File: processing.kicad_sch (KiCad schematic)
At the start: 58 parts, among them IC4 MT29F2G01ABAGDWB-IT_G_TR, IC5 MT29F2G01ABAGDWB-IT_G_TR, IC6 XMC7200D-E272K8384AA, IC7 DS90LV011AHMF_NOPB, Q1 ZXT849K, Y1 DSC1101DM2-012.0000, Y2 DSC1101DM2-125.0000T

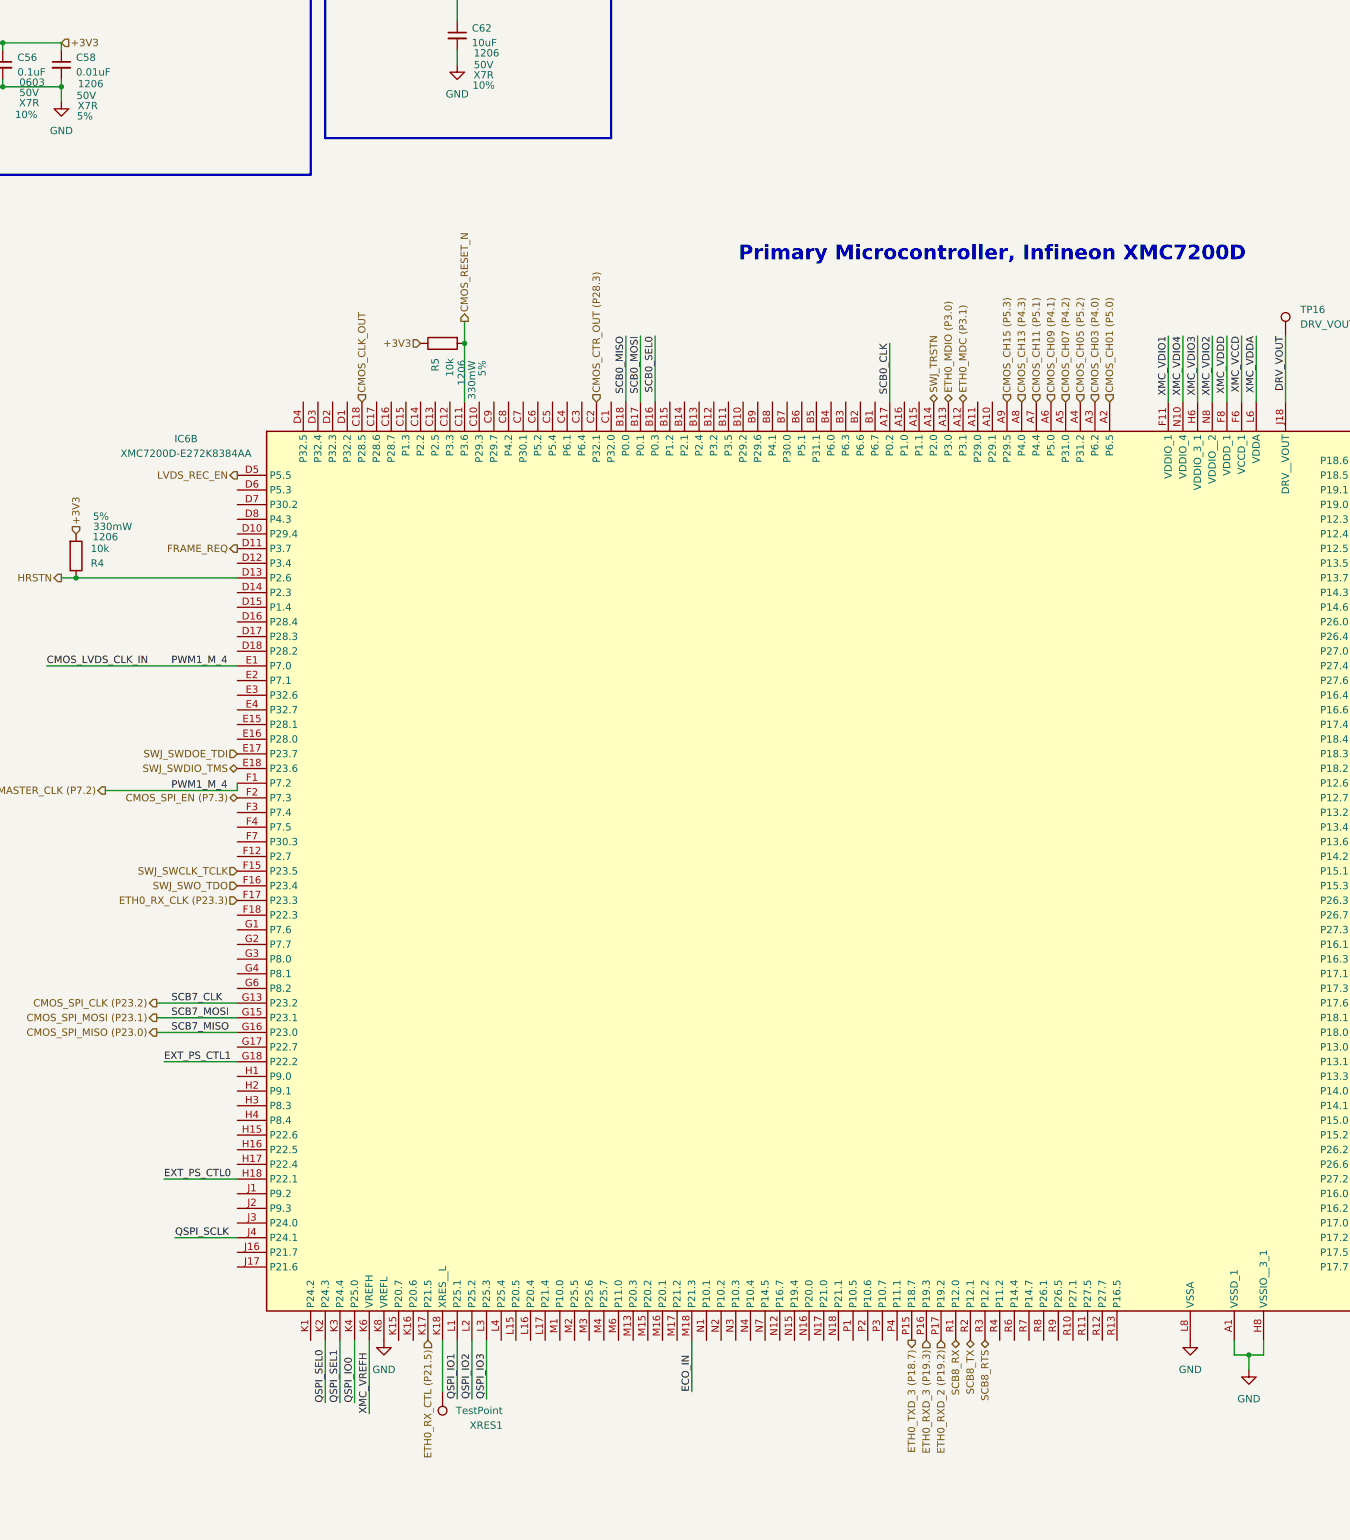
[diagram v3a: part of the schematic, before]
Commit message: Ready to order
Still unsure about 100uF cap
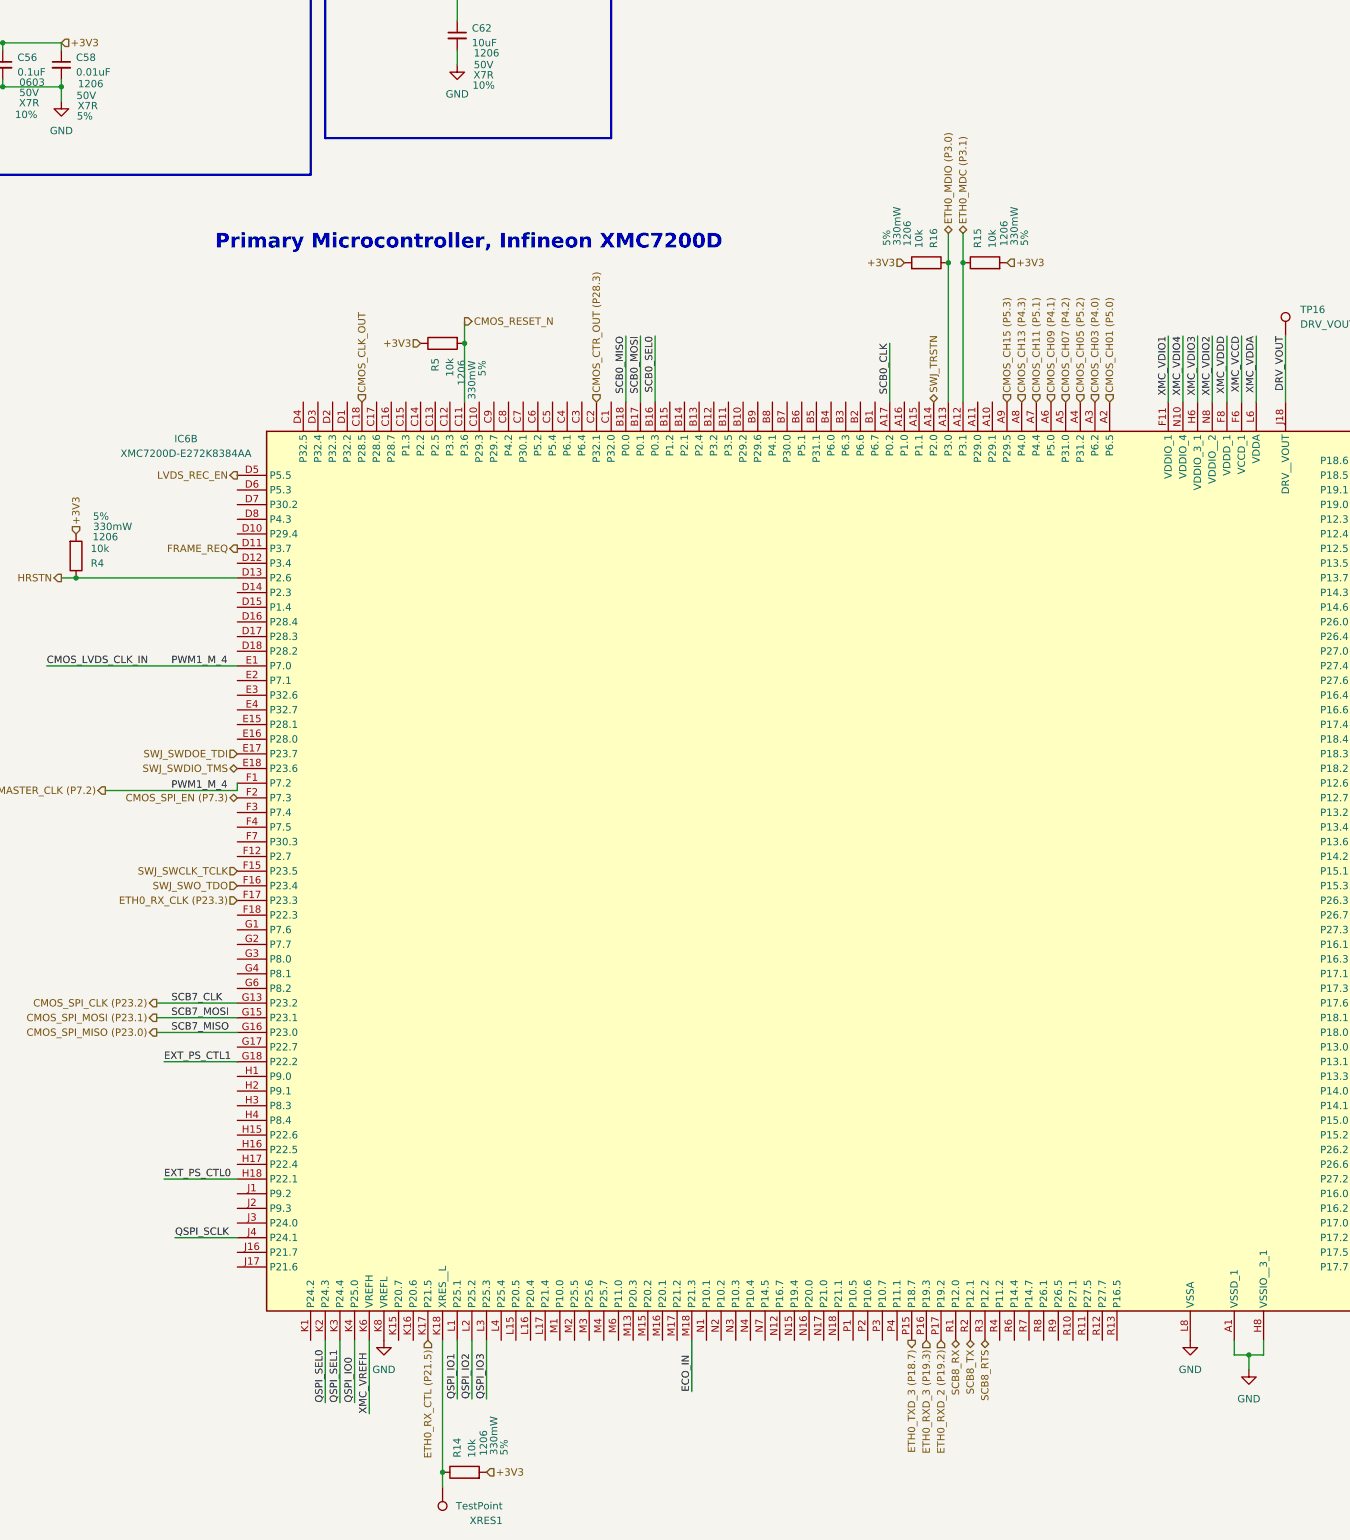
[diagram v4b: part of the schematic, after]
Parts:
- added R14, R15, R16: 10k, Resistor_SMD:R_1206_3216Metric, symbol Device:R
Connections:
- net +3V3: now also R14.2, R15.2, R16.2
- net ETH0_MDC (P3.1): now also R15.1
- net ETH0_MDIO (P3.0): now also R16.1
- net at IC6.K18 (XRES__L), XRES1.1: now also R14.1
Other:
- moved on the sheet: XRES1

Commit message: Labeled test pads; marked tantalums with lines for cathode; found suitable tantalum for 100 uF
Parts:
- DRV_VOUT1: renamed from TP16; value DRV_VOUT -> DRV_VOUT1
- renumbered TP15 to QSPI_IO0, TP11 to QSPI_IO1, TP12 to QSPI_IO2, TP13 to QSPI_IO3, TP14 to QSPI_SCLK1, TP10 to QSPI_SEL0, TP17 to QSPI_SEL1
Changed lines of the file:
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@@
 		(on_board yes)
 		(dnp no)
-		(fields_autoplaced yes)
-		(property "Reference" "TP15"
+		(property "Reference" "QSPI_IO0"
 			(at 93.98 113.0299 90)
 			(effects
@@
 			(project "S25-26"
 				(path "/6f4563ef-8a79-4567-b913-33c6dfb42b56/e295881b-793d-44b2-856b-25e9d19ba3af"
-					(reference "TP15")
+					(reference "QSPI_IO0")
 					(unit 1)
 				)
@@
 		(on_board yes)
 		(dnp no)
-		(fields_autoplaced yes)
-		(property "Reference" "TP13"
+		(property "Reference" "QSPI_IO3"
 			(at 93.98 105.4099 90)
 			(effects
@@
 			(project "S25-26"
 				(path "/6f4563ef-8a79-4567-b913-33c6dfb42b56/e295881b-793d-44b2-856b-25e9d19ba3af"
-					(reference "TP13")
+					(reference "QSPI_IO3")
 					(unit 1)
 				)
@@
 		(on_board yes)
 		(dnp no)
-		(fields_autoplaced yes)
-		(property "Reference" "TP17"
+		(property "Reference" "QSPI_SEL1"
 			(at 17.78 124.9679 0)
 			(effects
@@
 			(project "S25-26"
 				(path "/6f4563ef-8a79-4567-b913-33c6dfb42b56/e295881b-793d-44b2-856b-25e9d19ba3af"
-					(reference "TP17")
+					(reference "QSPI_SEL1")
 					(unit 1)
 				)
@@
 		(on_board yes)
 		(dnp no)
-		(fields_autoplaced yes)
-		(property "Reference" "TP10"
+		(property "Reference" "QSPI_SEL0"
 			(at 17.78 95.7579 0)
 			(effects
@@
 			(project "S25-26"
 				(path "/6f4563ef-8a79-4567-b913-33c6dfb42b56/e295881b-793d-44b2-856b-25e9d19ba3af"
-					(reference "TP10")
+					(reference "QSPI_SEL0")
 					(unit 1)
 				)
@@
 		(on_board yes)
 		(dnp no)
-		(fields_autoplaced yes)
-		(property "Reference" "TP12"
+		(property "Reference" "QSPI_IO2"
 			(at 22.86 121.9199 90)
 			(effects
@@
 			(project "S25-26"
 				(path "/6f4563ef-8a79-4567-b913-33c6dfb42b56/e295881b-793d-44b2-856b-25e9d19ba3af"
-					(reference "TP12")
+					(reference "QSPI_IO2")
 					(unit 1)
 				)
@@
 		(on_board yes)
 		(dnp no)
-		(fields_autoplaced yes)
-		(property "Reference" "TP14"
+		(property "Reference" "QSPI_SCLK1"
 			(at 93.98 109.2199 90)
 			(effects
@@
 			(project "S25-26"
 				(path "/6f4563ef-8a79-4567-b913-33c6dfb42b56/e295881b-793d-44b2-856b-25e9d19ba3af"
-					(reference "TP14")
+					(reference "QSPI_SCLK1")
 					(unit 1)
 				)
@@
 		(on_board yes)
 		(dnp no)
-		(fields_autoplaced yes)
-		(property "Reference" "TP11"
+		(property "Reference" "QSPI_IO1"
 			(at 17.78 117.6019 0)
 			(effects
@@
 			(project "S25-26"
 				(path "/6f4563ef-8a79-4567-b913-33c6dfb42b56/e295881b-793d-44b2-856b-25e9d19ba3af"
-					(reference "TP11")
+					(reference "QSPI_IO1")
 					(unit 1)
 				)
@@
 		(on_board yes)
 		(dnp no)
-		(fields_autoplaced yes)
-		(property "Reference" "TP16"
+		(property "Reference" "DRV_VOUT1"
 			(at 375.92 107.1879 0)
 			(effects
@@
 			)
 		)
-		(property "Value" "DRV_VOUT"
+		(property "Value" "DRV_VOUT1"
 			(at 375.92 109.7279 0)
 			(effects
@@
 			(project "S25-26"
 				(path "/6f4563ef-8a79-4567-b913-33c6dfb42b56/e295881b-793d-44b2-856b-25e9d19ba3af"
-					(reference "TP16")
+					(reference "DRV_VOUT1")
 					(unit 1)
 				)

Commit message: Beginning of V3
Long way to go
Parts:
- Q1: footprint Package_TO_SOT_SMD:TO-252-3_TabPin4 -> CustomFootprintLibrary:TO-252-3_TabPin4
- R6: footprint Resistor_SMD:R_0805_2012Metric -> Resistor_SMD:R_1206_3216Metric
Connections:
- net XRES: now reaches IC6.K18 (XRES__L), R14.1, XRES1.1
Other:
- moved on the sheet: XRES1
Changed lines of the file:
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@@
 		)
 	)
+	(hierarchical_label "XRES"
+		(shape input)
+		(at 227.33 311.15 270)
+		(effects
+			(font
+				(size 1.27 1.27)
+			)
+			(justify right)
+		)
+	)
 	(hierarchical_label "+3V3"
 		(shape input)
@@
 			)
 		)
-		(property "Footprint" "Resistor_SMD:R_0805_2012Metric"
+		(property "Footprint" "Resistor_SMD:R_1206_3216Metric"
 			(at 228.092 45.72 90)
 			(effects
@@
 	(symbol
 		(lib_id "Connector:TestPoint")
-		(at 227.33 311.15 180)
+		(at 227.33 311.15 90)
 		(unit 1)
 		(exclude_from_sim no)
@@
 		(dnp no)
 		(property "Reference" "XRES1"
-			(at 237.744 316.992 0)
+			(at 221.488 321.564 0)
 			(effects
 				(font
@@
 		)
 		(property "Value" "TestPoint"
-			(at 237.744 314.452 0)
+			(at 224.028 321.564 0)
 			(effects
 				(font
@@
 		)
 		(property "Footprint" "TestPoint:TestPoint_Pad_D1.0mm"
-			(at 222.25 311.15 0)
+			(at 227.33 306.07 0)
 			(effects
 				(font
@@
 		)
 		(property "Datasheet" "~"
-			(at 222.25 311.15 0)
+			(at 227.33 306.07 0)
 			(effects
 				(font
@@
 			)
 		)
-		(property "Footprint" "Package_TO_SOT_SMD:TO-252-3_TabPin4"
+		(property "Footprint" "CustomFootprintLibrary:TO-252-3_TabPin4"
 			(at 290.83 33.02 0)
 			(effects

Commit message: Excluded TPs from BOM
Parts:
- DRV_VOUT1, QSPI_IO0, QSPI_IO1, QSPI_IO2, QSPI_IO3, QSPI_SCLK1, QSPI_SEL0, QSPI_SEL1: now left out of the parts list
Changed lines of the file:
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@@
 		(unit 1)
 		(exclude_from_sim no)
-		(in_bom yes)
+		(in_bom no)
 		(on_board yes)
 		(dnp no)
@@
 				)
 				(justify left)
+				(hide yes)
 			)
 		)
@@
 		(unit 1)
 		(exclude_from_sim no)
-		(in_bom yes)
+		(in_bom no)
 		(on_board yes)
 		(dnp no)
@@
 				)
 				(justify left)
+				(hide yes)
 			)
 		)
@@
 		(unit 1)
 		(exclude_from_sim no)
-		(in_bom yes)
+		(in_bom no)
 		(on_board yes)
 		(dnp no)
@@
 				)
 				(justify left)
+				(hide yes)
 			)
 		)
@@
 		(unit 1)
 		(exclude_from_sim no)
-		(in_bom yes)
+		(in_bom no)
 		(on_board yes)
 		(dnp no)
@@
 				)
 				(justify left)
+				(hide yes)
 			)
 		)
@@
 		(unit 1)
 		(exclude_from_sim no)
-		(in_bom yes)
+		(in_bom no)
 		(on_board yes)
 		(dnp no)
@@
 				)
 				(justify left)
+				(hide yes)
 			)
 		)
@@
 		(unit 1)
 		(exclude_from_sim no)
-		(in_bom yes)
+		(in_bom no)
 		(on_board yes)
 		(dnp no)
@@
 				)
 				(justify left)
+				(hide yes)
 			)
 		)
@@
 		(unit 1)
 		(exclude_from_sim no)
-		(in_bom yes)
+		(in_bom no)
 		(on_board yes)
 		(dnp no)
@@
 				)
 				(justify right)
+				(hide yes)
 			)
 		)
@@
 		(unit 1)
 		(exclude_from_sim no)
-		(in_bom yes)
+		(in_bom no)
 		(on_board yes)
 		(dnp no)
@@
 				)
 				(justify left)
+				(hide yes)
 			)
 		)

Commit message: V3 Overhaul
Things remaining:
Ethernet Transceiver Clocks
Output Filtering on DC-DC Converter
Update some part numbers
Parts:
- removed R14, R4: 10k, Resistor_SMD:R_1206_3216Metric, symbol Device:R
- added C80: 15pF, Capacitor_SMD:C_0805_2012Metric, symbol Device:C
- added C81: 0.1uF, Capacitor_SMD:C_1206_3216Metric, symbol Device:C_Polarized
- added Y3: DSC1101DM2-025.0000, SamacSys_Parts:DSC1101DM20120000, symbol SamacSys_Parts:DSC1101DM2-012.0000
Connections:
- net +3V3: now also C81.1, Y3.6 (VDD); no longer R5.1
- net CMOS_MASTER_CLK (P7.2): no longer IC6.E1 (P7.0), IC7.5 (TTL_IN)
- net ETH0_REF_CLK (P18.0): no longer C78.1, Y2.4 (OUT)
- net GND: now also R5.1, C80.2, C81.2, Y3.3 (GND)
- new net CMOS_LVDS_CLK_IN: IC6.E1 (P7.0), IC7.5 (TTL_IN)
- new net GTX_CLK: C78.1, Y2.4 (OUT)
- new net XTAL_IN: C80.1, Y3.4 (OUT)
- no-connect marks 4 -> 6
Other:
- note added: "125MHz Oscillator"
